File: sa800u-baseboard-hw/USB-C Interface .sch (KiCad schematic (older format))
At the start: 8 parts

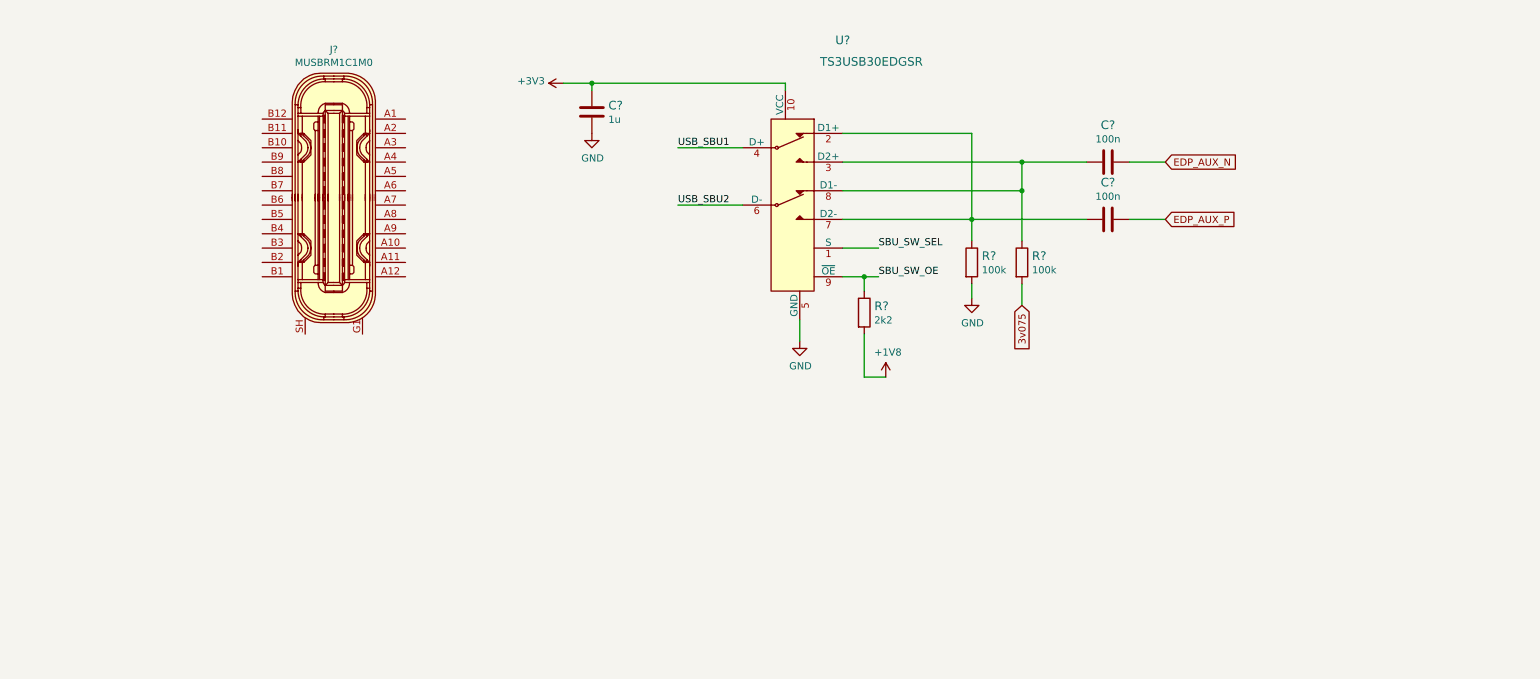
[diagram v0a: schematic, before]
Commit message: added usb type - c connector
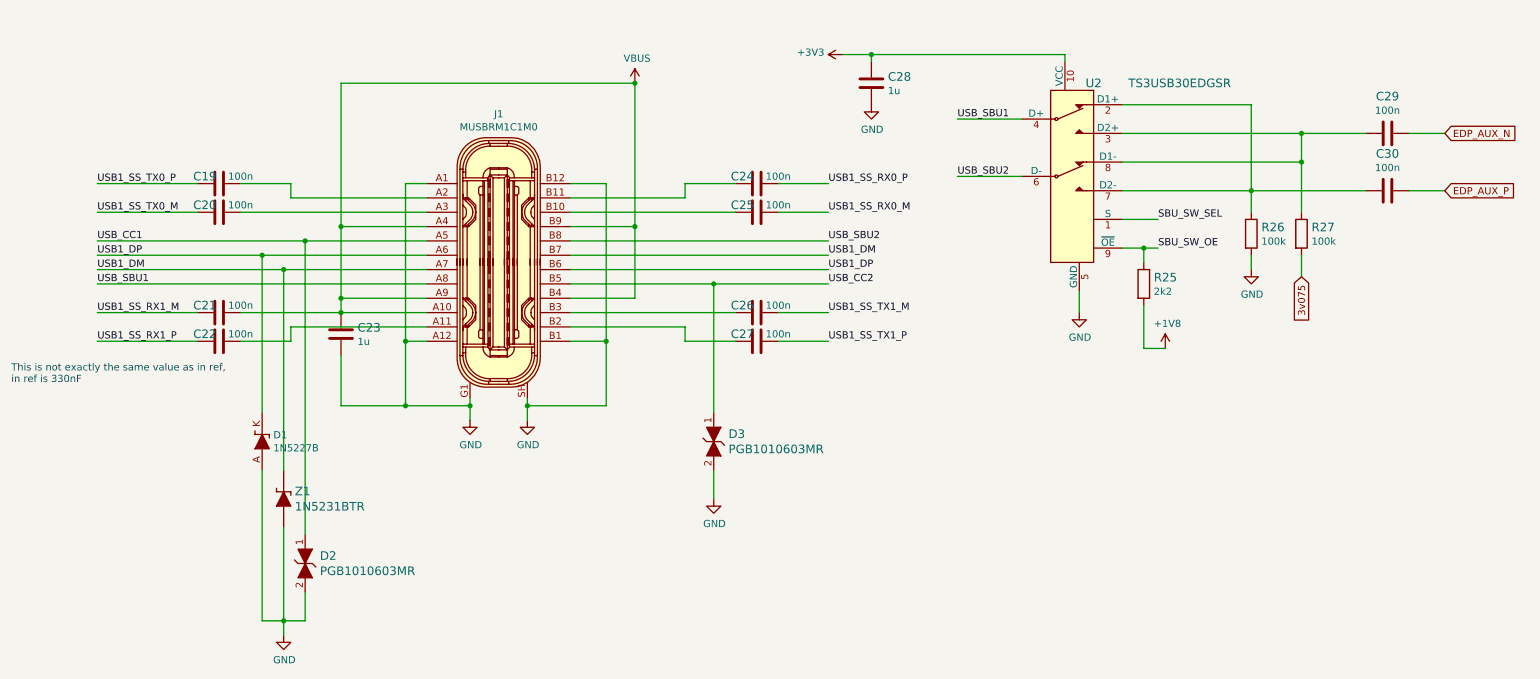
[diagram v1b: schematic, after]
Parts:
- added C19, C20, C21, C22, C24, C25, C26, C27: C_100n_0402, antmicro-footprints:0402-cap, symbol antmicroCapacitors0402:C_100n_0402
- added C23: C_1u_0402, antmicro-footprints:0402-cap, symbol antmicroCapacitors0402:C_1u_0402
- added D1: 1N5227B, symbol ZenerDiode:1N5227B
- added D2, D3: PGB1010603MR, antmicro-footprints:PGB1010603MR, symbol antmicroTVSDiodes:PGB1010603MR
- added Z1: 1N5231BTR, antmicro-footprints:DO-35, symbol antmicroDiodesZenerSingle:1N5231BTR
- gave numbers to parts that had none: 8
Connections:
- net GND: now also J1.A1, J1.A12, J1.B1, J1.B12, J1.G1, J1.SH, C23.2, D1.A, D2.2, D3.2, Z1.A
- net USB_SBU1: now also J1.A8
- net USB_SBU2: now also J1.B8
- net VBUS: now reaches J1.A10
- net VBUS: now also J1.A4, J1.A9, J1.B4, J1.B9, C21.1, C23.1
- net at J1.A11: now also C22.1
- net at J1.A2: now also C19.1
- net at J1.A3: now also C20.1
- net USB_CC1: now reaches J1.A5
- net USB_CC1: now also D2.1
- net USB1_DP: now reaches J1.A6
- net USB1_DP: now also J1.B6, D1.K
- net USB1_DM: now reaches J1.A7
- net USB1_DM: now also J1.B7, Z1.K
- net at J1.B10: now also C25.2
- net at J1.B11: now also C24.2
- net at J1.B2: now also C27.2
- net at J1.B3: now also C26.2
- net USB_CC2: now reaches J1.B5
- net USB_CC2: now also D3.1
- new net USB1_SS_RX0_M: C25.1
- new net USB1_SS_RX0_P: C24.1
- new net USB1_SS_RX1_M: C21.2
- new net USB1_SS_RX1_P: C22.2
- new net USB1_SS_TX0_M: C20.2
- new net USB1_SS_TX0_P: C19.2
- new net USB1_SS_TX1_M: C26.1
- new net USB1_SS_TX1_P: C27.1
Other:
- note added: "This is not exactly the same value as in ref,\nin ref is 330nF"
- moved on the sheet: C28, C29, C30, J1, R25, R26, R27, U2

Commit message: added 2 DSI connectors
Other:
- note added: "This should be optional,\nhard to get component and\nnot necessary."
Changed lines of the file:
@@
 $Descr A4 11693 8268
 encoding utf-8
-Sheet 5 5
+Sheet 5 6
 Title ""
 Date ""
@@
 	1    0    0    -1
 $EndComp
+Text Notes 7500 1050 0    50   ~ 0
+This should be optional,\nhard to get component and\nnot necessary.
 $EndSCHEMATC
